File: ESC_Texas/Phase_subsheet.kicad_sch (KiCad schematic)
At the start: 14 parts, among them IC8 AD8411AWBRZ, IC9 MC78L05ACHT1G, J10 Conn_01x03_Pin, J9 Conn_01x03_Pin

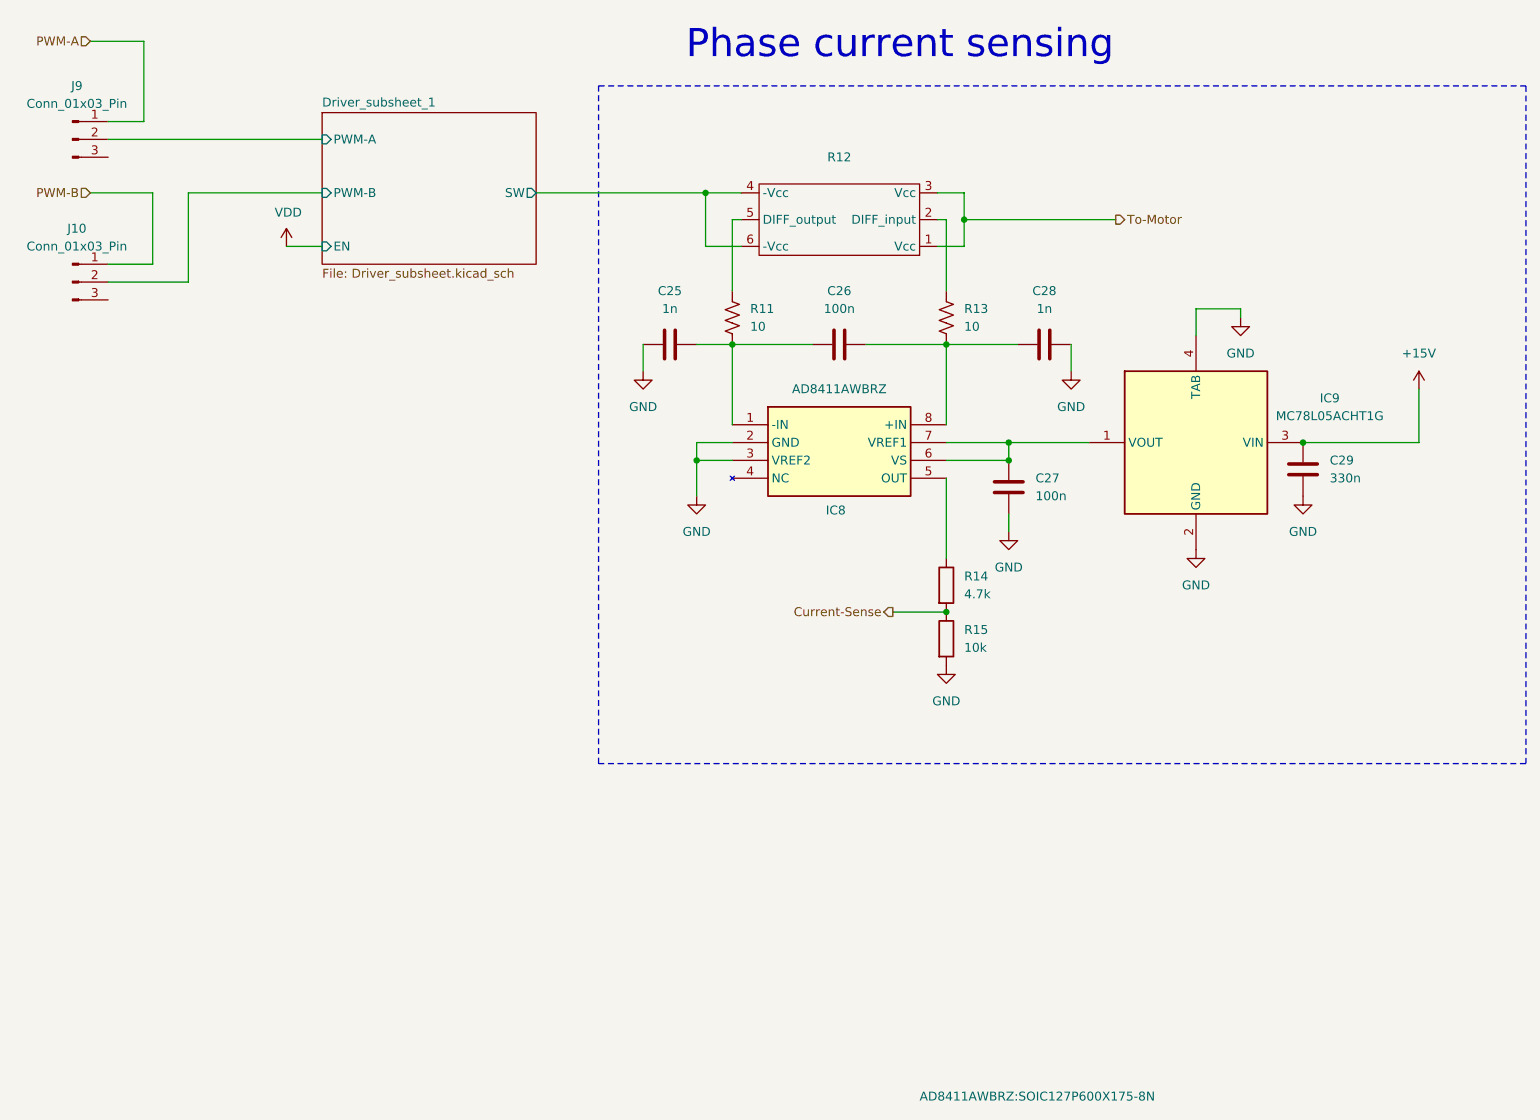
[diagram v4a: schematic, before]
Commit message: Changed hall connector
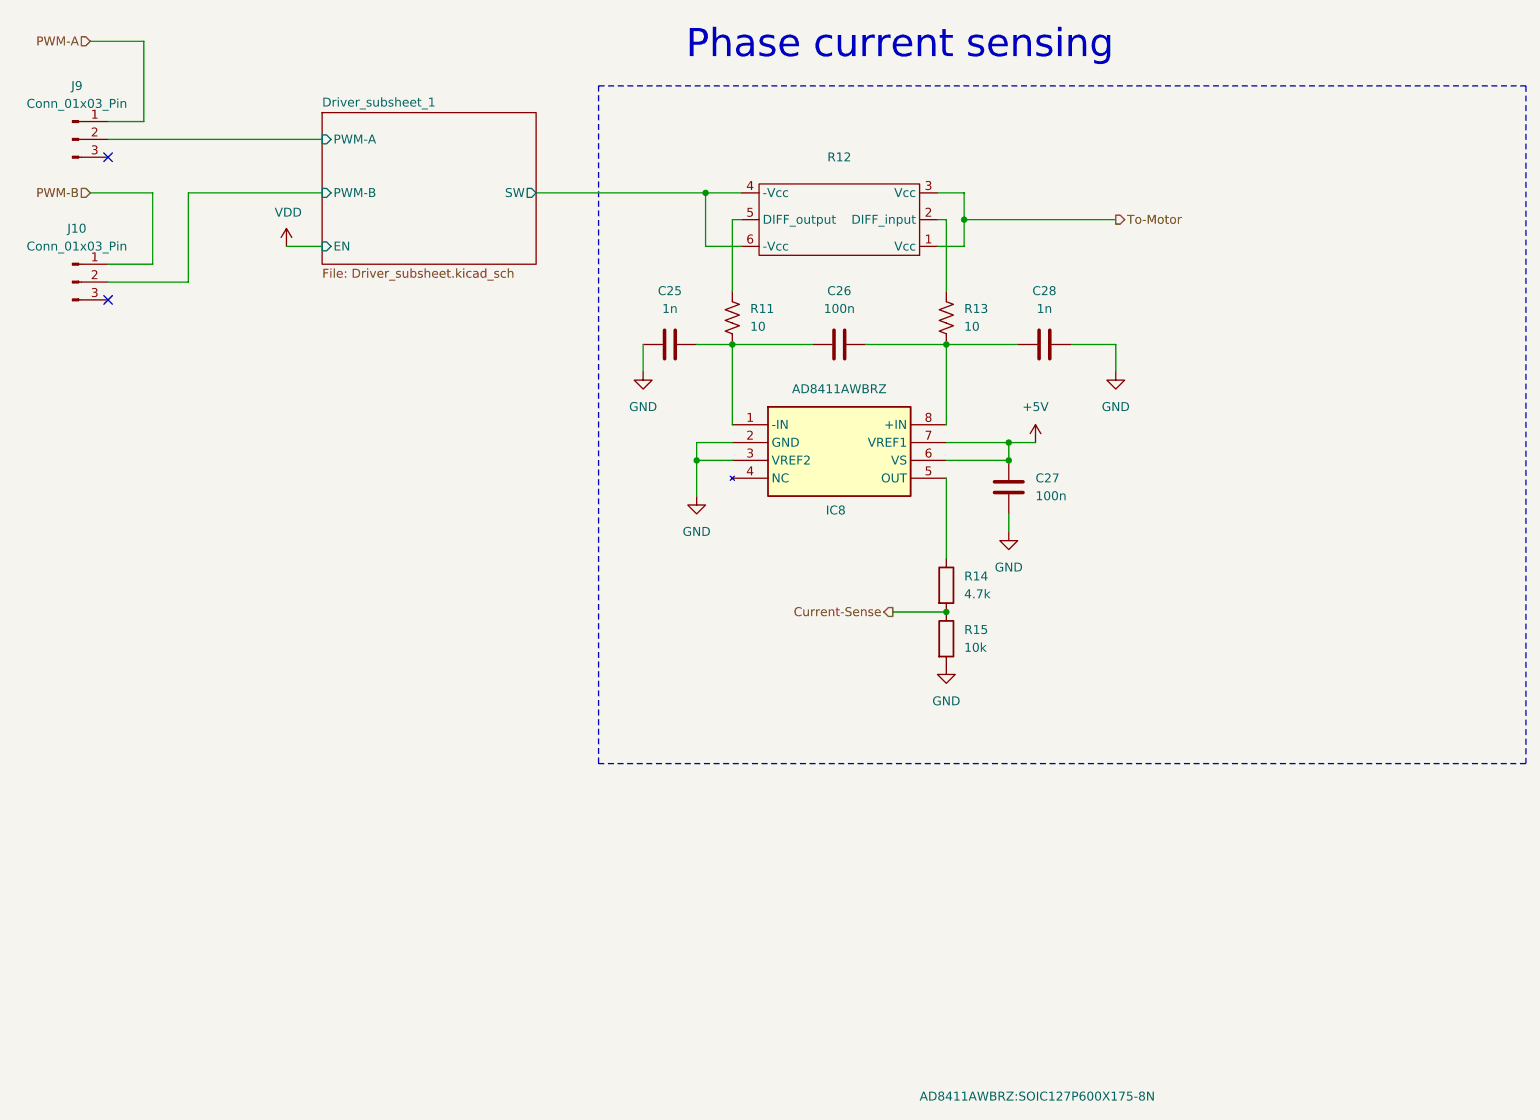
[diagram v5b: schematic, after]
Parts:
- removed C29: 330n, Capacitor_SMD:C_0805_2012Metric, symbol Device:C
- removed IC9: MC78L05ACHT1G, MC78L05ACHT1G:MC78L05ACHX_1, symbol MC78L05ACHT1G:MC78L05ACHT1G
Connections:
- net +5V: now reaches C27.1, IC8.6 (VS), IC8.7 (VREF1)
- no-connect marks 0 -> 2

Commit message: filters
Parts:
- added C24: F, Capacitor_SMD:C_0805_2012Metric, symbol Device:C
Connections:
- net Current-Sense: now also C24.1
- net GND: now also C24.2
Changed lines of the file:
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@@
+	)
+	(junction
+		(at 166.37 134.62)
+		(diameter 0)
+		(color 0 0 0 0)
 	)
 	(junction
@@
 	(wire
 		(pts
-			(xy 175.26 134.62) (xy 182.88 134.62)
+			(xy 160.02 134.62) (xy 166.37 134.62)
 		)
 		(stroke
@@
 		(pts
 			(xy 182.88 115.57) (xy 182.88 127)
+		)
+		(stroke
+			(width 0)
+			(type default)
+		)
+	)
+	(wire
+		(pts
+			(xy 166.37 134.62) (xy 182.88 134.62)
 		)
 		(stroke
@@
 	(hierarchical_label "Current-Sense"
 		(shape output)
-		(at 175.26 134.62 180)
+		(at 160.02 134.62 180)
 		(fields_autoplaced yes)
 		(effects
@@
 	)
 	(symbol
+		(lib_id "Device:C")
+		(at 166.37 138.43 0)
+		(unit 1)
+		(exclude_from_sim no)
+		(in_bom yes)
+		(on_board yes)
+		(dnp no)
+		(fields_autoplaced yes)
+		(property "Reference" "C24"
+			(at 170.18 137.1599 0)
+			(effects
+				(font
+					(size 1.27 1.27)
+				)
+				(justify left)
+			)
+		)
+		(property "Value" "F"
+			(at 170.18 139.6999 0)
+			(effects
+				(font
+					(size 1.27 1.27)
+				)
+				(justify left)
+			)
+		)
+		(property "Footprint" "Capacitor_SMD:C_0805_2012Metric"
+			(at 167.3352 142.24 0)
+			(effects
+				(font
+					(size 1.27 1.27)
+				)
+				(hide yes)
+			)
+		)
+		(property "Datasheet" "~"
+			(at 166.37 138.43 0)
+			(effects
+				(font
+					(size 1.27 1.27)
+				)
+				(hide yes)
+			)
+		)
+		(property "Description" "Unpolarized capacitor"
+			(at 166.37 138.43 0)
+			(effects
+				(font
+					(size 1.27 1.27)
+				)
+				(hide yes)
+			)
+		)
+		(pin "2"
+		)
+		(pin "1"
+		)
+		(instances
+			(project "ESC_Texas"
+				(path "/0e3a5351-d2cd-4ecc-a1be-cca9c5f62ea0/553690e4-0a20-4b8e-821c-55ba3788d3c5"
+					(reference "C50")
+					(unit 1)
+				)
+				(path "/0e3a5351-d2cd-4ecc-a1be-cca9c5f62ea0/63c8dce8-451d-41ee-b438-d688cf3e64bd"
+					(reference "C29")
+					(unit 1)
+				)
+				(path "/0e3a5351-d2cd-4ecc-a1be-cca9c5f62ea0/b8e552f6-93a8-4098-a907-a65be165d984"
+					(reference "C24")
+					(unit 1)
+				)
+			)
+		)
+	)
+	(symbol
 		(lib_id "Device:R_US")
 		(at 152.4 92.71 0)
@@
 					(unit 1)
 				)
+			)
+		)
+	)
+	(symbol
+		(lib_id "power:GND")
+		(at 166.37 142.24 0)
+		(unit 1)
+		(exclude_from_sim no)
+		(in_bom yes)
+		(on_board yes)
+		(dnp no)
+		(fields_autoplaced yes)
+		(property "Reference" "#PWR045"
+			(at 166.37 148.59 0)
+			(effects
+				(font
+					(size 1.27 1.27)
+				)
+				(hide yes)
+			)
+		)
+		(property "Value" "GND"
+			(at 166.37 147.32 0)
+			(effects
+				(font
+					(size 1.27 1.27)
+				)
+			)
+		)
+		(property "Footprint" ""
+			(at 166.37 142.24 0)
+			(effects
+				(font
+					(size 1.27 1.27)
+				)
+				(hide yes)
+			)
+		)
+		(property "Datasheet" ""
+			(at 166.37 142.24 0)
+			(effects
+				(font
+					(size 1.27 1.27)
+				)
+				(hide yes)
+			)
+		)
+		(property "Description" "Power symbol creates a global label with name \"GND\" , ground"
+			(at 166.37 142.24 0)
+			(effects
+				(font
+					(size 1.27 1.27)
+				)
+				(hide yes)
+			)
+		)
+		(pin "1"
+		)
+		(instances
+			(project "ESC_Texas"
+				(path "/0e3a5351-d2cd-4ecc-a1be-cca9c5f62ea0/553690e4-0a20-4b8e-821c-55ba3788d3c5"
+					(reference "#PWR047")
+					(unit 1)
+				)
+				(path "/0e3a5351-d2cd-4ecc-a1be-cca9c5f62ea0/63c8dce8-451d-41ee-b438-d688cf3e64bd"
+					(reference "#PWR046")
+					(unit 1)
+				)
+				(path "/0e3a5351-d2cd-4ecc-a1be-cca9c5f62ea0/b8e552f6-93a8-4098-a907-a65be165d984"
+					(reference "#PWR045")
+					(unit 1)
+				)
